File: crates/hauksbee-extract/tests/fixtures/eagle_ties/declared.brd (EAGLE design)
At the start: 0 parts

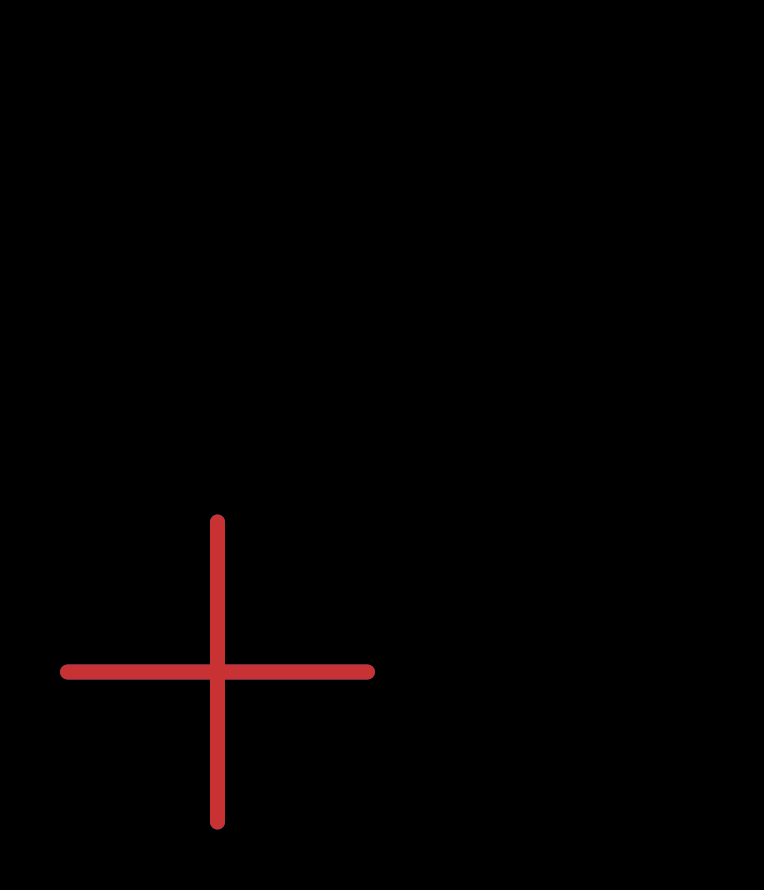
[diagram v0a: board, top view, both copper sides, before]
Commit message: Fix Eagle schematic net-tie parity
Require physical vertical copper and canonical pin/net identity before qualifying Eagle contacts. Preserve the established APIs while carrying optional schematic evidence through CLI, TUI, reports, standalone web analysis, and live launch.
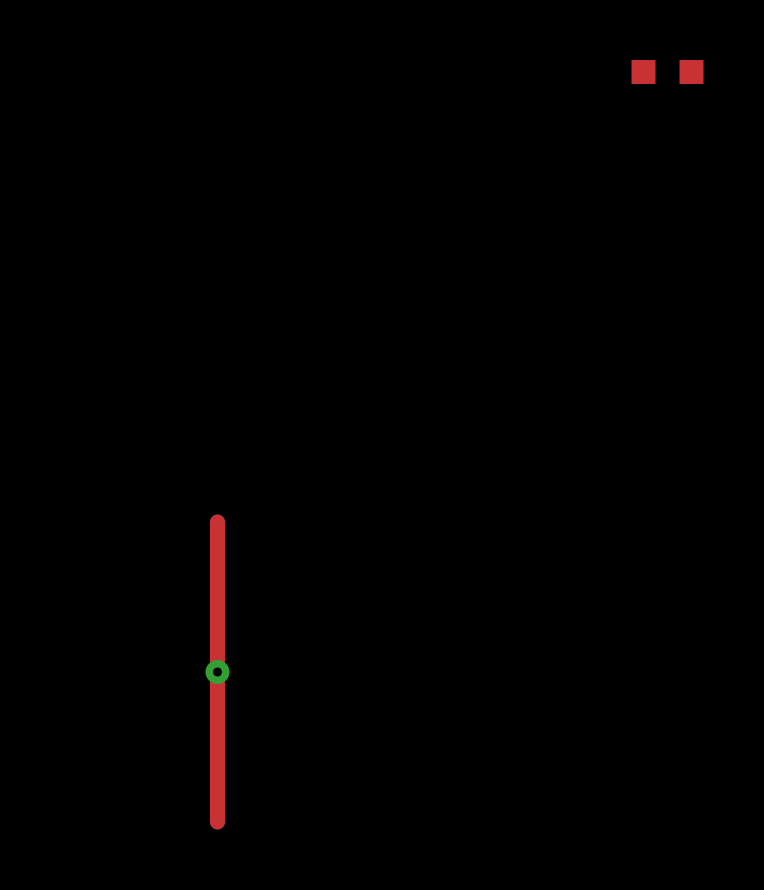
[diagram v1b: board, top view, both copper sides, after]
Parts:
- added R1: 10k, device:R0603
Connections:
- new net AGND: R1.2
- new net GND: R1.1
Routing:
- net GND: track 20.0 -> 0.00 mm, vias 0 -> 1
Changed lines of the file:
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@@
 <eagle version="6.6.0"><drawing><layers>
 <layer number="1" name="Top"/><layer number="16" name="Bottom"/>
-</layers><board><libraries/><designrules name="default">
+</layers><board><designrules name="default">
 <param name="mdWireWire" value="6mil"/><param name="mdWirePad" value="6mil"/>
 <param name="mdPadPad" value="6mil"/><param name="mdSmdSmd" value="6mil"/>
-</designrules><elements/><signals>
-<signal name="GND"><wire x1="0" y1="0" x2="10" y2="0" width="0.5" layer="1"/><wire x1="0" y1="0" x2="10" y2="0" width="0.5" layer="16"/></signal>
-<signal name="AGND"><wire x1="5" y1="-5" x2="5" y2="5" width="0.5" layer="1"/><wire x1="5" y1="-5" x2="5" y2="5" width="0.5" layer="16"/></signal>
+</designrules><elements><element name="R1" library="device" package="R0603" value="10k" x="20" y="20"/></elements><signals>
+<signal name="GND"><contactref element="R1" pad="1"/><via x="5" y="0" extent="1-16" drill="0.3" diameter="0.8"/></signal>
+<signal name="AGND"><contactref element="R1" pad="2"/><wire x1="5" y1="-5" x2="5" y2="5" width="0.5" layer="1"/><wire x1="5" y1="-5" x2="5" y2="5" width="0.5" layer="16"/></signal>
 </signals></board></drawing></eagle>
